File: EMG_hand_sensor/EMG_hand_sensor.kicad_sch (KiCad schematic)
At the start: 42 parts, among them J1 Conn_2Rows-07Pins_Shielded, J2 B2B-XH-A, U1 TVS0500DRV, U2 ADA4099-1xUJ, U3 CD74HC4067M, U4 ADA4099-1xUJ, U5 ADA4099-1xUJ, U8 ADA4099-1xUJ, U9 0A

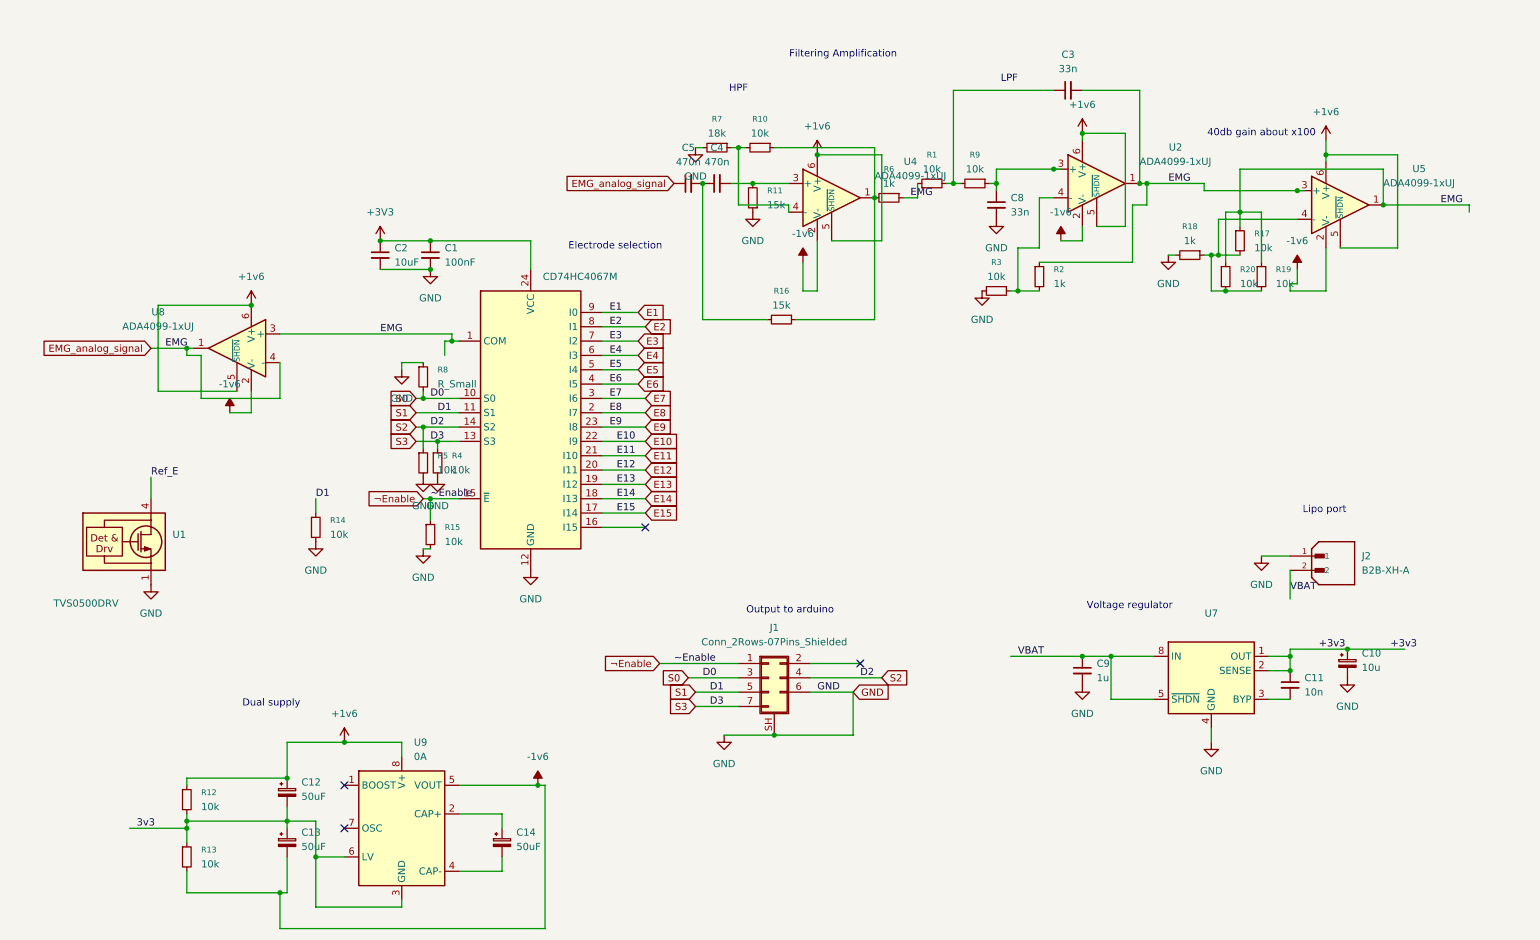
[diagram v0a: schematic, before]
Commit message: finished with first schematic for now
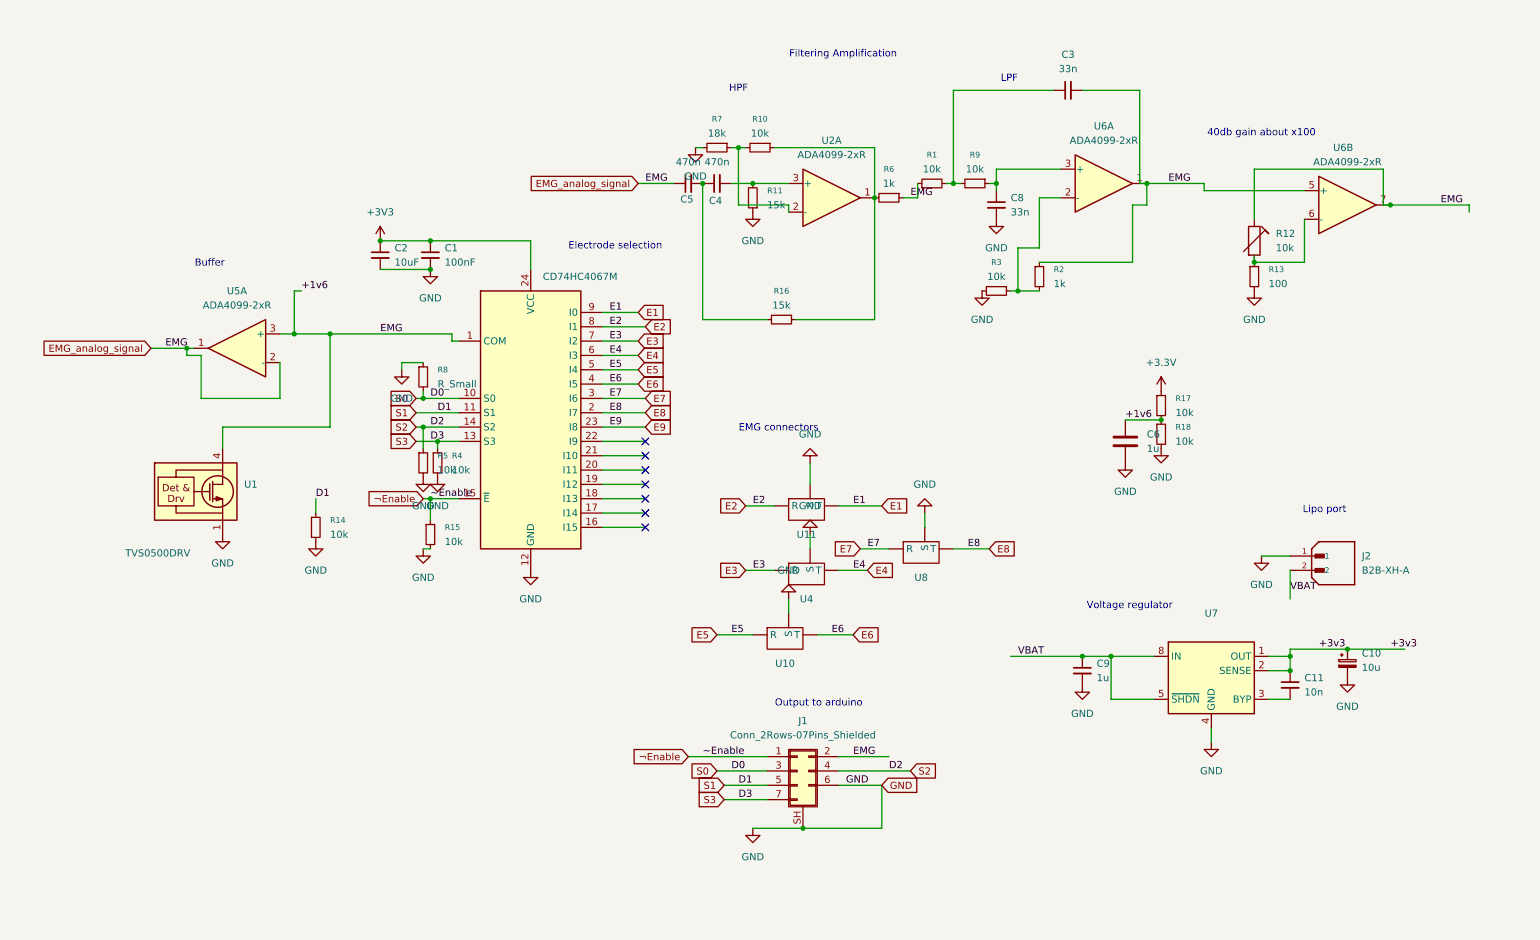
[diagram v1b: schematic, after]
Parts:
- removed C12, C13, C14: 50uF, symbol Device:C_Polarized_Small
- removed R12, R19, R20: 10k, symbol Device:R_Small
- removed U2, U4, U5, U8: ADA4099-1xUJ, Package_TO_SOT_SMD:TSOT-23-6, symbol Amplifier_Operational:ADA4099-1xUJ
- removed U9: 0A, Package_SO:SOIC-8_3.9x4.9mm_P1.27mm, symbol Converter_DCDC:TC7662Bx0A
- added C6: 1u, symbol Device:C
- added R12: 10k, symbol Device:R_Trim
- added U10, U11, U4, U8: ~, Connector_Audio:Jack_3.5mm_CUI_SJ-3523-SMT_Horizontal, symbol Audio_connector:TRS_connn
- added U2, U5, U6: ADA4099-2xR, Package_SO:SOIC-8_3.9x4.9mm_P1.27mm, symbol Amplifier_Operational:ADA4099-2xR
- J1: footprint (none) -> Connector_PinHeader_2.54mm:PinHeader_1x07_P2.54mm_Vertical_SMD_Pin1Left
- J2: footprint (none) -> Connector_JST:JST_EH_B2B-EH-A_1x02_P2.50mm_Vertical
- R13: value 10k -> 100
- R18: value 1k -> 10k
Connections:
- net -1v6 is gone; now on net GND: R13.2
- net Ref_E is gone; now on net EMG_analog_signal: U1.4 (IN), U1.5 (IN), U1.6 (IN)
- net E1: now also U11. (T)
- net E2: now also U11. (T)
- net E3: now also U4. (T)
- net E4: now also U4. (T)
- net E5: now also U10. (T)
- net E6: now also U10. (T)
- net E7: now also U8. (T)
- net E8: now also U8. (T)
- net EMG_analog_signal: now also J1.2 (Pin_2), R17.2, R18.1, C6.1, R12.1, U5.1, U5.2 (-), U5.3 (+), U6.1, U6.5 (+), U6.7; no longer R17.1
- net GND: now also C6.2, U10. (T), U11. (T), U4. (T), U8. (T)
- net at R10.1, R16.1, R6.2: now also U2.1
- net at C4.2, R11.2: now also U2.3 (+)
- net at R10.2, R7.1: now also U2.2 (-)
- net at R2.2, R3.1: now also U6.2 (-)
- net at C8.1, R9.1: now also U6.3 (+)
- net 3v3: no longer names the net of R13.1
- net 3v3: now also R12.2, U6.6 (-)
- net E10: no longer names the net of U3.22 (I9)
- net E11: no longer names the net of U3.21 (I10)
- net E12: no longer names the net of U3.20 (I11)
- net E13: no longer names the net of U3.19 (I12)
- net E14: no longer names the net of U3.18 (I13)
- net E15: no longer names the net of U3.17 (I14)
- new net +3.3V: R17.1
- no-connect marks 4 -> 7
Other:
- note added: "Buffer"
- note added: "EMG connectors"
- note removed: "Dual supply"
- moved on the sheet: J1, U1

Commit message: starting pcb design
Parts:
- C1, C2: footprint (none) -> Capacitor_SMD:C_0805_2012Metric_Pad1.18x1.45mm_HandSolder
- C10: value 10u -> 10uF; footprint (none) -> Capacitor_THT:CP_Radial_D6.3mm_P2.50mm
- C11: value 10n -> 10nF; footprint (none) -> Capacitor_SMD:C_0805_2012Metric_Pad1.18x1.45mm_HandSolder
- C3, C8: value 33n -> 33nF; footprint (none) -> Capacitor_SMD:C_0805_2012Metric_Pad1.18x1.45mm_HandSolder
- C4, C5: value 470n -> 470nF; footprint (none) -> Capacitor_SMD:C_0805_2012Metric_Pad1.18x1.45mm_HandSolder
- C6, C9: value 1u -> 1uF; footprint (none) -> Capacitor_SMD:C_0805_2012Metric_Pad1.18x1.45mm_HandSolder
- R1, R10, R11, R12, R14, R15, R16, R17, R18, R2, R3, R4, R5, R6, R7, R9: footprint (none) -> Resistor_SMD:R_0805_2012Metric_Pad1.20x1.40mm_HandSolder
- R13: value 100 -> 100R; footprint (none) -> Resistor_SMD:R_0805_2012Metric_Pad1.20x1.40mm_HandSolder
- R8: value R_Small -> 10k; footprint (none) -> Resistor_SMD:R_0805_2012Metric_Pad1.20x1.40mm_HandSolder
- U10, U11, U4, U8: value ~ -> TRS_AUDIO_JACK_3.5mm
- U7: value ~ -> LT1762
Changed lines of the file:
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@@
 			)
 		)
-		(property "Value" "10n"
+		(property "Value" "10nF"
 			(at 241.3 137.1662 0)
 			(effects
@@
 			)
 		)
-		(property "Footprint" ""
+		(property "Footprint" "Capacitor_SMD:C_0805_2012Metric_Pad1.18x1.45mm_HandSolder"
 			(at 238.76 135.89 0)
 			(effects
@@
 			)
 		)
-		(property "Footprint" ""
+		(property "Footprint" "Capacitor_SMD:C_0805_2012Metric_Pad1.18x1.45mm_HandSolder"
 			(at 86.36 59.69 0)
 			(effects
@@
 			)
 		)
-		(property "Value" "R_Small"
+		(property "Value" "10k"
 			(at 87.63 82.5499 0)
 			(effects
@@
 			)
 		)
-		(property "Footprint" ""
+		(property "Footprint" "Resistor_SMD:R_0805_2012Metric_Pad1.20x1.40mm_HandSolder"
 			(at 85.09 81.28 0)
 			(effects
@@
 			)
 		)
-		(property "Footprint" ""
+		(property "Footprint" "Resistor_SMD:R_0805_2012Metric_Pad1.20x1.40mm_HandSolder"
 			(at 85.09 96.52 0)
 			(effects
@@
 			)
 		)
-		(property "Value" "470n"
+		(property "Value" "470nF"
 			(at 137.1663 43.18 90)
 			(effects
@@
 			)
 		)
-		(property "Footprint" ""
+		(property "Footprint" "Capacitor_SMD:C_0805_2012Metric_Pad1.18x1.45mm_HandSolder"
 			(at 137.16 46.99 0)
 			(effects
@@
 			)
 		)
-		(property "Footprint" ""
+		(property "Footprint" "Resistor_SMD:R_0805_2012Metric_Pad1.20x1.40mm_HandSolder"
 			(at 186.69 66.04 0)
 			(effects
@@
 			)
 		)
-		(property "Footprint" ""
+		(property "Footprint" "Resistor_SMD:R_0805_2012Metric_Pad1.20x1.40mm_HandSolder"
 			(at 175.26 46.99 0)
 			(effects
@@
 			)
 		)
-		(property "Footprint" ""
+		(property "Footprint" "Resistor_SMD:R_0805_2012Metric_Pad1.20x1.40mm_HandSolder"
 			(at 194.31 63.5 0)
 			(effects
@@
 			)
 		)
-		(property "Footprint" ""
+		(property "Footprint" "Resistor_SMD:R_0805_2012Metric_Pad1.20x1.40mm_HandSolder"
 			(at 87.63 96.52 0)
 			(effects
@@
 			)
 		)
-		(property "Footprint" ""
+		(property "Footprint" "Resistor_SMD:R_0805_2012Metric_Pad1.20x1.40mm_HandSolder"
 			(at 167.64 49.53 0)
 			(effects
@@
 			)
 		)
-		(property "Footprint" ""
+		(property "Footprint" "Resistor_SMD:R_0805_2012Metric_Pad1.20x1.40mm_HandSolder"
 			(at 215.9 91.44 0)
 			(effects
@@
 			)
 		)
-		(property "Value" "~"
+		(property "Value" "TRS_AUDIO_JACK_3.5mm"
 			(at 149.225 133.35 0)
 			(effects
@@
 			)
 		)
-		(property "Footprint" ""
+		(property "Footprint" "Resistor_SMD:R_0805_2012Metric_Pad1.20x1.40mm_HandSolder"
 			(at 86.36 109.22 0)
 			(effects
@@
 			)
 		)
-		(property "Footprint" ""
+		(property "Footprint" "Resistor_SMD:R_0805_2012Metric_Pad1.20x1.40mm_HandSolder"
 			(at 143.51 49.53 0)
 			(effects
@@
 			)
 		)
-		(property "Footprint" ""
+		(property "Footprint" "Resistor_SMD:R_0805_2012Metric_Pad1.20x1.40mm_HandSolder"
 			(at 148.59 71.12 0)
 			(effects
@@
 			)
 		)
-		(property "Footprint" ""
+		(property "Footprint" "Resistor_SMD:R_0805_2012Metric_Pad1.20x1.40mm_HandSolder"
 			(at 230.632 57.15 90)
 			(effects
@@
 			)
 		)
-		(property "Footprint" ""
+		(property "Footprint" "Resistor_SMD:R_0805_2012Metric_Pad1.20x1.40mm_HandSolder"
 			(at 66.04 107.95 0)
 			(effects
@@
 			)
 		)
-		(property "Value" "1u"
+		(property "Value" "1uF"
 			(at 213.36 93.9799 0)
 			(effects
@@
 			)
 		)
-		(property "Footprint" ""
+		(property "Footprint" "Capacitor_SMD:C_0805_2012Metric_Pad1.18x1.45mm_HandSolder"
 			(at 210.5152 96.52 0)
 			(effects
@@
 			)
 		)
-		(property "Value" "33n"
+		(property "Value" "33nF"
 			(at 199.3963 26.67 90)
 			(effects
@@
 			)
 		)
-		(property "Footprint" ""
+		(property "Footprint" "Capacitor_SMD:C_0805_2012Metric_Pad1.18x1.45mm_HandSolder"
 			(at 199.39 30.48 0)
 			(effects
@@
 			)
 		)
-		(property "Value" "~"
+		(property "Value" "TRS_AUDIO_JACK_3.5mm"
 			(at 153.035 121.92 0)
 			(effects
@@
 			)
 		)
-		(property "Value" "~"
+		(property "Value" "TRS_AUDIO_JACK_3.5mm"
 			(at 173.355 118.11 0)
 			(effects
@@
 			)
 		)
-		(property "Value" "1u"
+		(property "Value" "1uF"
 			(at 204.47 134.6262 0)
 			(effects
@@
 			)
 		)
-		(property "Footprint" ""
+		(property "Footprint" "Capacitor_SMD:C_0805_2012Metric_Pad1.18x1.45mm_HandSolder"
 			(at 201.93 133.35 0)
 			(effects
@@
 			)
 		)
-		(property "Value" "470n"
+		(property "Value" "470nF"
 			(at 132.0863 43.18 90)
 			(effects
@@
 			)
 		)
-		(property "Footprint" ""
+		(property "Footprint" "Capacitor_SMD:C_0805_2012Metric_Pad1.18x1.45mm_HandSolder"
 			(at 132.08 46.99 0)
 			(effects
@@
 			)
 		)
-		(property "Value" "~"
+		(property "Value" "TRS_AUDIO_JACK_3.5mm"
 			(at 153.035 110.49 0)
 			(effects
@@
 			)
 		)
-		(property "Value" "~"
+		(property "Value" "LT1762"
 			(at 224.79 125.73 0)
 			(effects
@@
 			)
 		)
-		(property "Value" "10u"
+		(property "Value" "10uF"
 			(at 251.46 132.8038 0)
 			(effects
@@
 			)
 		)
-		(property "Footprint" ""
+		(property "Footprint" "Capacitor_THT:CP_Radial_D6.3mm_P2.50mm"
 			(at 248.92 132.08 0)
 			(effects
@@
 			)
 		)
-		(property "Value" "33n"
+		(property "Value" "33nF"
 			(at 189.23 52.0762 0)
 			(effects
@@
 			)
 		)
-		(property "Footprint" ""
+		(property "Footprint" "Capacitor_SMD:C_0805_2012Metric_Pad1.18x1.45mm_HandSolder"
 			(at 186.69 50.8 0)
 			(effects
@@
 			)
 		)
-		(property "Value" "100"
+		(property "Value" "100R"
 			(at 234.95 64.7699 0)
 			(effects
@@
 			)
 		)
-		(property "Footprint" ""
+		(property "Footprint" "Resistor_SMD:R_0805_2012Metric_Pad1.20x1.40mm_HandSolder"
 			(at 232.41 63.5 0)
 			(effects
@@
 			)
 		)
-		(property "Footprint" ""
+		(property "Footprint" "Resistor_SMD:R_0805_2012Metric_Pad1.20x1.40mm_HandSolder"
 			(at 137.16 40.64 0)
 			(effects
@@
 			)
 		)
-		(property "Footprint" ""
+		(property "Footprint" "Resistor_SMD:R_0805_2012Metric_Pad1.20x1.40mm_HandSolder"
 			(at 144.78 40.64 0)
 			(effects
@@
 			)
 		)
-		(property "Footprint" ""
+		(property "Footprint" "Resistor_SMD:R_0805_2012Metric_Pad1.20x1.40mm_HandSolder"
 			(at 215.9 86.36 0)
 			(effects
@@
 			)
 		)
-		(property "Footprint" ""
+		(property "Footprint" "Resistor_SMD:R_0805_2012Metric_Pad1.20x1.40mm_HandSolder"
 			(at 182.88 46.99 0)
 			(effects
@@
 			)
 		)
-		(property "Footprint" ""
+		(property "Footprint" "Capacitor_SMD:C_0805_2012Metric_Pad1.18x1.45mm_HandSolder"
 			(at 77.47 59.69 0)
 			(effects

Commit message: component placement and design rules
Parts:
- removed U5: ADA4099-2xR, Package_SO:SOIC-8_3.9x4.9mm_P1.27mm, symbol Amplifier_Operational:ADA4099-2xR
- added unit 2 of U2
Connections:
- net EMG_analog_signal: now also U2.1, U2.2 (-), U2.3 (+)
- net at C4.2, R11.2: now also U2.5 (+); no longer U2.3 (+)
- net at R10.1, R16.1, R6.2: now also U2.7; no longer U2.1
- net at R10.2, R7.1: now also U2.6 (-); no longer U2.2 (-)
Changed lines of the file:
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@@
 	)
 	(symbol
+		(lib_id "Amplifier_Operational:ADA4099-2xR")
+		(at 52.07 76.2 0)
+		(mirror y)
+		(unit 1)
+		(exclude_from_sim no)
+		(in_bom yes)
+		(on_board yes)
+		(dnp no)
+		(property "Reference" "U2"
+			(at 52.07 66.04 0)
+			(effects
+				(font
+					(size 1.27 1.27)
+				)
+			)
+		)
+		(property "Value" "ADA4099-2xR"
+			(at 52.07 68.58 0)
+			(effects
+				(font
+					(size 1.27 1.27)
+				)
+			)
+		)
+		(property "Footprint" "Package_SO:SOIC-8_3.9x4.9mm_P1.27mm"
+			(at 49.53 76.2 0)
+			(effects
+				(font
+					(size 1.27 1.27)
+				)
+				(hide yes)
+			)
+		)
+		(property "Datasheet" "https://www.analog.com/media/en/technical-documentation/data-sheets/ada4099-1_ada4099-2.pdf"
+			(at 45.72 72.39 0)
+			(effects
+				(font
+					(size 1.27 1.27)
+				)
+				(hide yes)
+			)
+		)
+		(property "Description" "3.15..50V supply, 8MHz GBW, Rail-to-Rail input/output, over-the-top dual opamp, SOIC-8"
+			(at 52.07 76.2 0)
+			(effects
+				(font
+					(size 1.27 1.27)
+				)
+				(hide yes)
+			)
+		)
+		(pin "5"
+		)
+		(pin "4"
+		)
+		(pin "7"
+		)
+		(pin "8"
+		)
+		(pin "3"
+		)
+		(pin "2"
+		)
+		(pin "1"
+		)
+		(pin "6"
+		)
+		(instances
+			(project ""
+				(path "/84a42da6-643f-42bf-9876-7927dca3da2c"
+					(reference "U2")
+					(unit 1)
+				)
+			)
+		)
+	)
+	(symbol
 		(lib_id "Device:R_Small")
 		(at 186.69 66.04 270)
@@
 	)
 	(symbol
-		(lib_id "Amplifier_Operational:ADA4099-2xR")
-		(at 157.48 49.53 0)
-		(unit 1)
-		(exclude_from_sim no)
-		(in_bom yes)
-		(on_board yes)
-		(dnp no)
-		(fields_autoplaced yes)
-		(property "Reference" "U2"
-			(at 157.48 39.37 0)
-			(effects
-				(font
-					(size 1.27 1.27)
-				)
-			)
-		)
-		(property "Value" "ADA4099-2xR"
-			(at 157.48 41.91 0)
-			(effects
-				(font
-					(size 1.27 1.27)
-				)
-			)
-		)
-		(property "Footprint" "Package_SO:SOIC-8_3.9x4.9mm_P1.27mm"
-			(at 160.02 49.53 0)
-			(effects
-				(font
-					(size 1.27 1.27)
-				)
-				(hide yes)
-			)
-		)
-		(property "Datasheet" "https://www.analog.com/media/en/technical-documentation/data-sheets/ada4099-1_ada4099-2.pdf"
-			(at 163.83 45.72 0)
-			(effects
-				(font
-					(size 1.27 1.27)
-				)
-				(hide yes)
-			)
-		)
-		(property "Description" "3.15..50V supply, 8MHz GBW, Rail-to-Rail input/output, over-the-top dual opamp, SOIC-8"
-			(at 157.48 49.53 0)
-			(effects
-				(font
-					(size 1.27 1.27)
-				)
-				(hide yes)
-			)
-		)
-		(pin "7"
-		)
-		(pin "5"
-		)
-		(pin "4"
-		)
-		(pin "2"
-		)
-		(pin "6"
-		)
-		(pin "3"
-		)
-		(pin "8"
-		)
-		(pin "1"
-		)
-		(instances
-			(project "EMG_hand_sensor"
-				(path "/84a42da6-643f-42bf-9876-7927dca3da2c"
-					(reference "U2")
-					(unit 1)
-				)
-			)
-		)
-	)
-	(symbol
 		(lib_id "Device:R_Small")
 		(at 215.9 91.44 0)
@@
 	)
 	(symbol
+		(lib_id "Amplifier_Operational:ADA4099-2xR")
+		(at 157.48 49.53 0)
+		(unit 2)
+		(exclude_from_sim no)
+		(in_bom yes)
+		(on_board yes)
+		(dnp no)
+		(fields_autoplaced yes)
+		(property "Reference" "U2"
+			(at 157.48 39.37 0)
+			(effects
+				(font
+					(size 1.27 1.27)
+				)
+			)
+		)
+		(property "Value" "ADA4099-2xR"
+			(at 157.48 41.91 0)
+			(effects
+				(font
+					(size 1.27 1.27)
+				)
+			)
+		)
+		(property "Footprint" "Package_SO:SOIC-8_3.9x4.9mm_P1.27mm"
+			(at 160.02 49.53 0)
+			(effects
+				(font
+					(size 1.27 1.27)
+				)
+				(hide yes)
+			)
+		)
+		(property "Datasheet" "https://www.analog.com/media/en/technical-documentation/data-sheets/ada4099-1_ada4099-2.pdf"
+			(at 163.83 45.72 0)
+			(effects
+				(font
+					(size 1.27 1.27)
+				)
+				(hide yes)
+			)
+		)
+		(property "Description" "3.15..50V supply, 8MHz GBW, Rail-to-Rail input/output, over-the-top dual opamp, SOIC-8"
+			(at 157.48 49.53 0)
+			(effects
+				(font
+					(size 1.27 1.27)
+				)
+				(hide yes)
+			)
+		)
+		(pin "2"
+		)
+		(pin "1"
+		)
+		(pin "6"
+		)
+		(pin "5"
+		)
+		(pin "3"
+		)
+		(pin "7"
+		)
+		(pin "8"
+		)
+		(pin "4"
+		)
+		(instances
+			(project ""
+				(path "/84a42da6-643f-42bf-9876-7927dca3da2c"
+					(reference "U2")
+					(unit 2)
+				)
+			)
+		)
+	)
+	(symbol
 		(lib_id "Device:C_Small")
 		(at 199.39 30.48 90)
@@
 					(unit 1)
 				)
-			)
-		)
-	)
-	(symbol
-		(lib_id "Amplifier_Operational:ADA4099-2xR")
-		(at 52.07 76.2 0)
-		(mirror y)
-		(unit 1)
-		(exclude_from_sim no)
-		(in_bom yes)
-		(on_board yes)
-		(dnp no)
-		(property "Reference" "U5"
-			(at 52.07 66.04 0)
-			(effects
-				(font
-					(size 1.27 1.27)
-				)
-			)
-		)
-		(property "Value" "ADA4099-2xR"
-			(at 52.07 68.58 0)
-			(effects
-				(font
-					(size 1.27 1.27)
-				)
-			)
-		)
-		(property "Footprint" "Package_SO:SOIC-8_3.9x4.9mm_P1.27mm"
-			(at 49.53 76.2 0)
-			(effects
-				(font
-					(size 1.27 1.27)
-				)
-				(hide yes)
-			)
-		)
-		(property "Datasheet" "https://www.analog.com/media/en/technical-documentation/data-sheets/ada4099-1_ada4099-2.pdf"
-			(at 45.72 72.39 0)
-			(effects
-				(font
-					(size 1.27 1.27)
-				)
-				(hide yes)
-			)
-		)
-		(property "Description" "3.15..50V supply, 8MHz GBW, Rail-to-Rail input/output, over-the-top dual opamp, SOIC-8"
-			(at 52.07 76.2 0)
-			(effects
-				(font
-					(size 1.27 1.27)
-				)
-				(hide yes)
-			)
-		)
-		(pin "7"
-		)
-		(pin "5"
-		)
-		(pin "4"
-		)
-		(pin "2"
-		)
-		(pin "6"
-		)
-		(pin "3"
-		)
-		(pin "8"
-		)
-		(pin "1"
-		)
-		(instances
-			(project "EMG_hand_sensor"
-				(path "/84a42da6-643f-42bf-9876-7927dca3da2c"
-					(reference "U5")
-					(unit 1)
-				)
